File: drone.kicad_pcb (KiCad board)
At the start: 2 copper layers, 99.3 x 99.3 mm, 43 parts, among them J1 Conn_01x02, J10 Conn_01x02, J2 Conn_01x02, J7 USB_B_Micro, J8 Conn_01x02, J9 Conn_01x02, Q5 BSS138, Q6 BSS138, U1 ESP32-WROOM-32, U10 DRV8231DDAR, U11 DRV8231DDAR, U2 MPU-6050, U3 DWM1000, U4 BMP280, U5 LM1117MP-3.3, U6 CH340C, U7 MMC5883MA, U8 DRV8231DDAR, U9 DRV8231DDAR

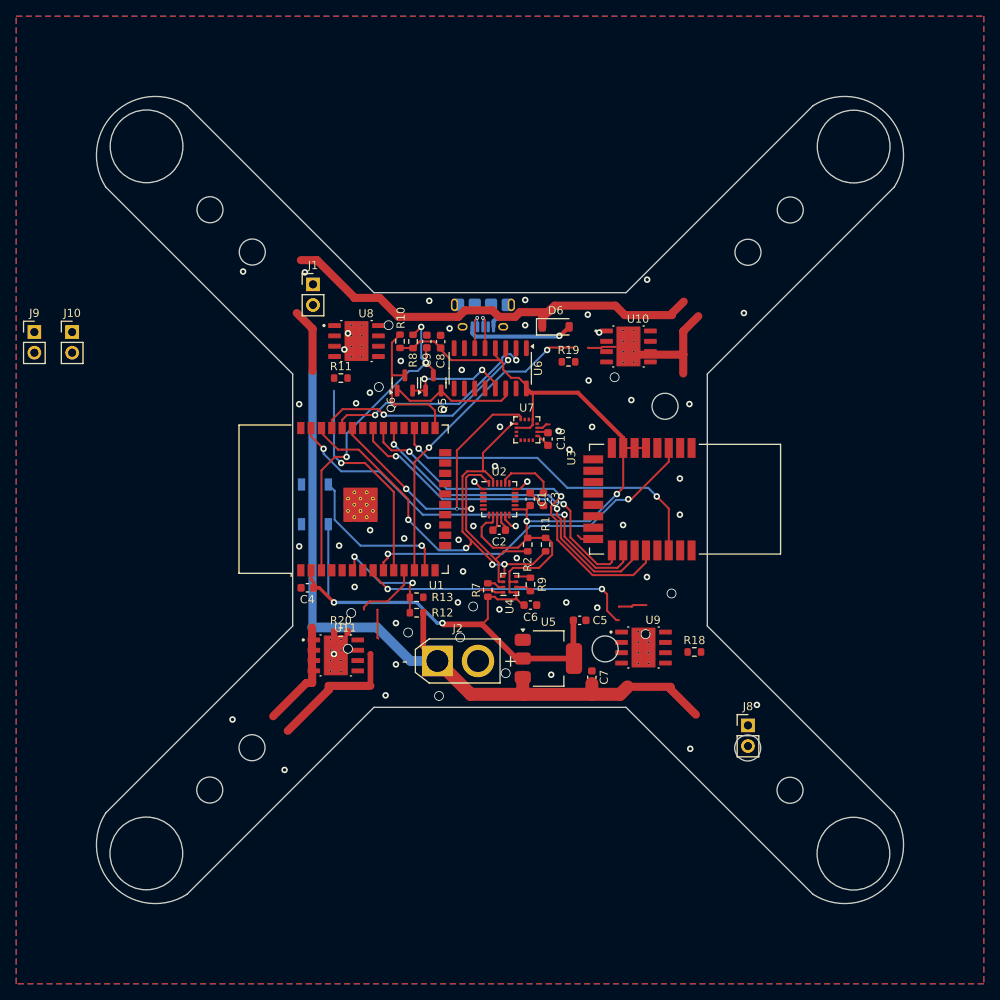
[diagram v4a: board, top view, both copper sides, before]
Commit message: add motor driver wiring on pcb
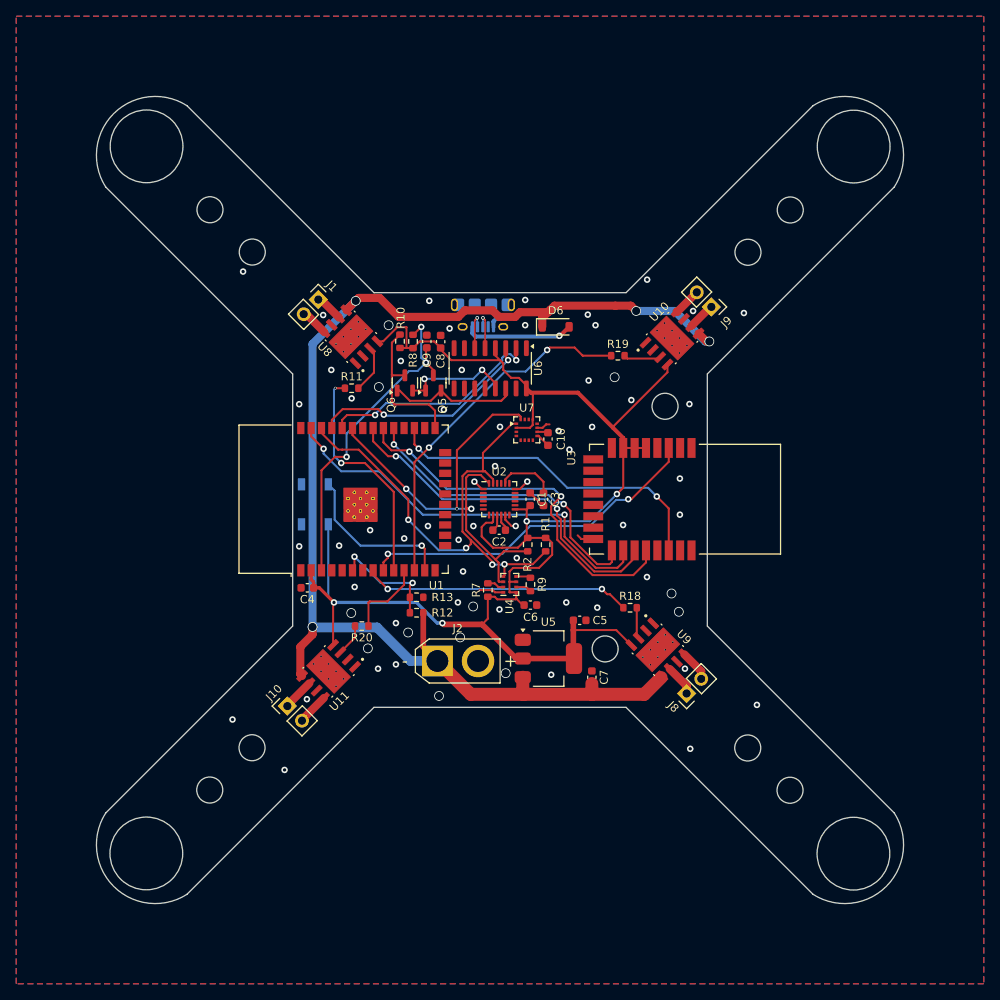
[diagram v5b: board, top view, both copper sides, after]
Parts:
- moved J9 83.3 mm to (126.5, 76.8), turned to -135 degrees
- moved J10 53.1 mm to (74.3, 125.8), turned to 45 degrees
- moved R18 9.60 mm to (116.5, 113.8)
- moved J8 8.51 mm to (123.5, 124.3), turned to 135 degrees
- moved R19 6.12 mm to (115.0, 82.8)
- moved U10 5.46 mm to (121.7, 80.6), turned to 45 degrees
- moved R20 2.68 mm to (83.5, 116.0), turned to 180 degrees
- moved U11 2.16 mm to (79.4, 121.6), turned to -135 degrees
- moved J1 1.98 mm to (78.2, 75.8), turned to -45 degrees
- moved R11 1.82 mm to (82.2, 86.8)
- moved U9 1.78 mm to (119.9, 118.9), turned to -45 degrees
- moved U8 0.87 mm to (82.2, 80.4), turned to 135 degrees
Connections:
- R18 pad 1: MOTOR_2 -> MOTOR_4
- R20 pad 1: MOTOR_4 -> MOTOR_2
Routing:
- net (no net): track 41.5 -> 0.00 mm
- net VCC: track 158.7 -> 189.3 mm
- net BAT+: track 173.0 -> 160.3 mm, vias 0 -> 4
- net Net-(U8-IN1): track 0.00 -> 5.87 mm
- net MOTOR_3: track 38.8 -> 43.8 mm
- net Net-(U10-IN1): track 0.00 -> 4.59 mm
- net Net-(U11-IN1): track 0.00 -> 3.97 mm
- net Net-(J10-Pin_2): track 0.00 -> 3.93 mm
- net Net-(J10-Pin_1): track 0.00 -> 3.93 mm
- net Net-(J8-Pin_1): track 0.00 -> 3.88 mm
- net Net-(J8-Pin_2): track 0.00 -> 3.88 mm
- net Net-(U9-IN1): track 0.00 -> 3.80 mm
- net Net-(J1-Pin_1): track 0.00 -> 3.47 mm
- net Net-(J1-Pin_2): track 0.00 -> 3.47 mm
- net Net-(J9-Pin_2): track 0.00 -> 3.46 mm
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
